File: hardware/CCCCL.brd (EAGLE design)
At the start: 58.1 x 54.6 mm, 31 parts, among them IC1 7805L, IC2 25LC040P, IC3 OPAMP-DUALDIP, J1 AVR_SPI_PRG_6NS

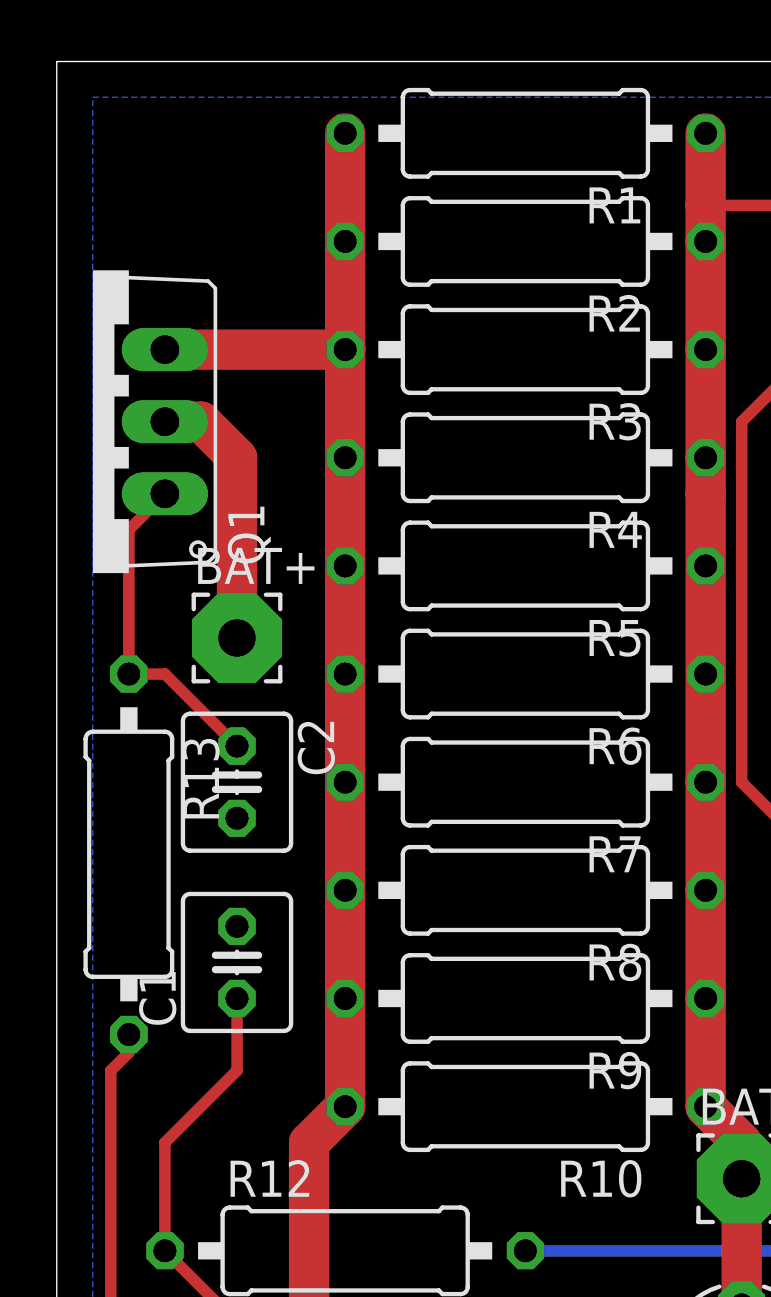
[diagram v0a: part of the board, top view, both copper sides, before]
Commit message: fixed up power routing
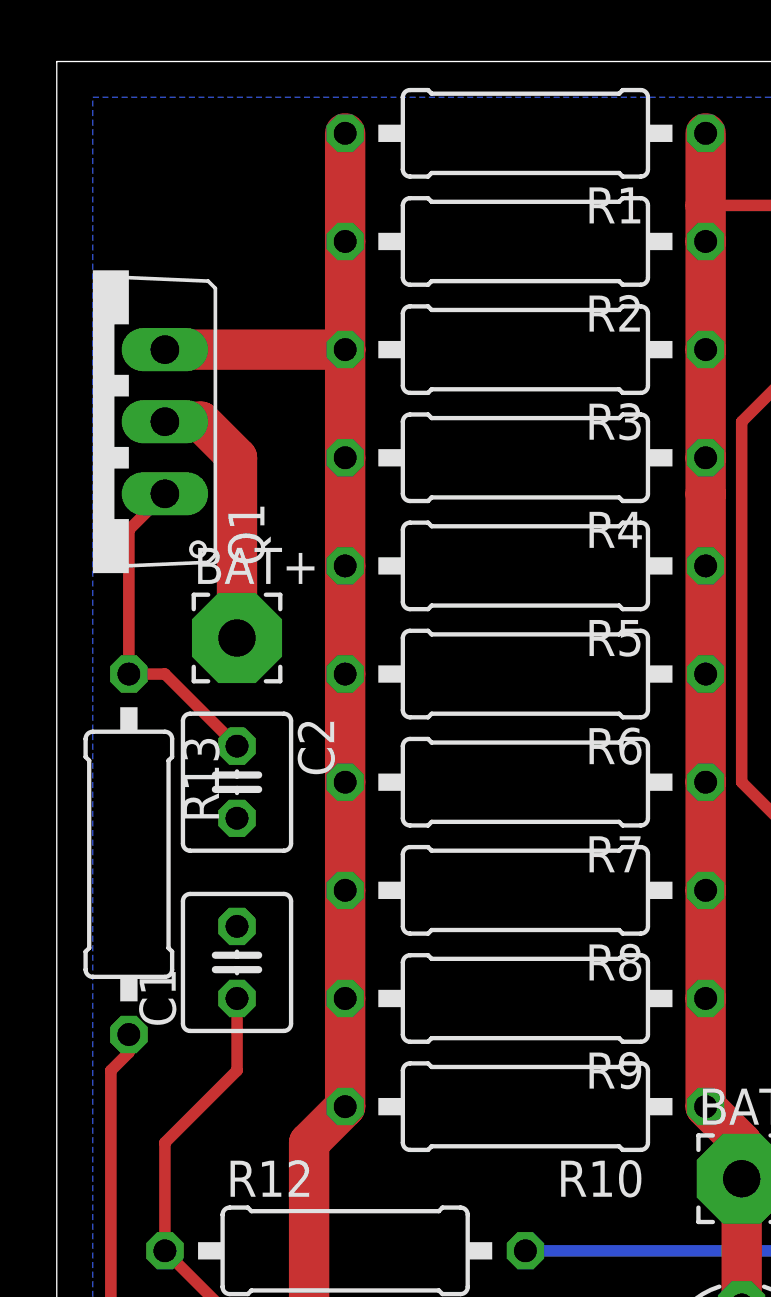
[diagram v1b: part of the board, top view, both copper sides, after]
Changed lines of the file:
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@@
 <contactref element="Q1" pad="3"/>
 <contactref element="IC3" pad="2"/>
-<wire x1="16.51" y1="74.93" x2="16.51" y2="67.31" width="1.4224" layer="1"/>
-<wire x1="16.51" y1="67.31" x2="16.51" y2="40.64" width="1.4224" layer="1"/>
+<wire x1="16.51" y1="71.12" x2="16.51" y2="67.31" width="1.4224" layer="1"/>
+<wire x1="16.51" y1="67.31" x2="16.51" y2="63.5" width="1.4224" layer="1"/>
+<wire x1="16.51" y1="48.26" x2="16.51" y2="44.45" width="1.4224" layer="1"/>
 <wire x1="15.24" y1="39.37" x2="16.51" y2="40.64" width="1.4224" layer="1"/>
 <wire x1="10.16" y1="67.31" x2="16.51" y2="67.31" width="1.4224" layer="1"/>
 <wire x1="15.24" y1="33.02" x2="15.24" y2="39.37" width="1.4224" layer="1"/>
-<wire x1="16.51" y1="74.93" x2="16.51" y2="71.12" width="0" layer="19" extent="1-1"/>
-<wire x1="16.51" y1="63.5" x2="16.51" y2="67.31" width="0" layer="19" extent="1-1"/>
-<wire x1="16.51" y1="59.69" x2="16.51" y2="63.5" width="0" layer="19" extent="1-1"/>
-<wire x1="16.51" y1="55.88" x2="16.51" y2="59.69" width="0" layer="19" extent="1-1"/>
-<wire x1="16.51" y1="52.07" x2="16.51" y2="55.88" width="0" layer="19" extent="1-1"/>
-<wire x1="16.51" y1="48.26" x2="16.51" y2="52.07" width="0" layer="19" extent="1-1"/>
-<wire x1="16.51" y1="44.45" x2="16.51" y2="40.64" width="0" layer="19" extent="1-1"/>
+<wire x1="16.51" y1="40.64" x2="16.51" y2="44.45" width="1.4224" layer="1"/>
+<wire x1="16.51" y1="48.26" x2="16.51" y2="52.07" width="1.4224" layer="1"/>
+<wire x1="16.51" y1="52.07" x2="16.51" y2="55.88" width="1.4224" layer="1"/>
+<wire x1="16.51" y1="55.88" x2="16.51" y2="59.69" width="1.4224" layer="1"/>
+<wire x1="16.51" y1="59.69" x2="16.51" y2="63.5" width="1.4224" layer="1"/>
+<wire x1="16.51" y1="71.12" x2="16.51" y2="74.93" width="1.4224" layer="1"/>
 </signal>
 <signal name="GND">
